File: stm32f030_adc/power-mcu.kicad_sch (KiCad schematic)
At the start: 24 parts, among them J4 Conn_01x05_Socket, U1 STM32F103C6Tx, U2 AMS1117-3.3, X1 USB_B_Micro, Y2 8 MHz

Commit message: [schematics] Impl |  Most of the work is done. Intermediate result
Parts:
- removed J4: Conn_01x05_Socket, Connector_PinHeader_2.00mm:PinHeader_1x05_P2.00mm_Vertical, symbol Connector:Conn_01x05_Socket
- added J1: Conn_01x03_Socket, Connector_PinHeader_1.00mm:PinHeader_1x03_P1.00mm_Vertical, symbol Connector:Conn_01x03_Socket
- added TP1, TP2: TestPoint, TestPoint:TestPoint_Pad_D2.0mm, symbol Connector:TestPoint
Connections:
- net GNDREF: now also J1.3 (Pin_3)
- net SWD_CLK: now also TP2.1
- net SWD_IO: now also TP1.1
- net USART_1_RX: now also J1.1 (Pin_1)
- net USART_1_TX: now also J1.2 (Pin_2)
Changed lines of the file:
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@@
 	(wire
 		(pts
+			(xy 219.71 120.65) (xy 229.87 120.65)
+		)
+		(stroke
+			(width 0)
+			(type default)
+		)
+	)
+	(wire
+		(pts
 			(xy 185.42 129.54) (xy 198.12 129.54)
 		)
@@
 	(wire
 		(pts
-			(xy 228.6 123.19) (xy 243.84 123.19)
+			(xy 229.87 123.19) (xy 222.25 123.19)
 		)
 		(stroke
@@
 	(wire
 		(pts
-			(xy 228.6 115.57) (xy 243.84 115.57)
-		)
-		(stroke
-			(width 0)
-			(type default)
-		)
-	)
-	(wire
-		(pts
 			(xy 193.04 82.55) (xy 207.01 82.55)
 		)
@@
 	(wire
 		(pts
-			(xy 228.6 118.11) (xy 243.84 118.11)
-		)
-		(stroke
-			(width 0)
-			(type default)
-		)
-	)
-	(wire
-		(pts
 			(xy 68.58 146.05) (xy 83.82 146.05)
 		)
@@
 	(wire
 		(pts
-			(xy 228.6 125.73) (xy 243.84 125.73)
-		)
-		(stroke
-			(width 0)
-			(type default)
-		)
-	)
-	(wire
-		(pts
 			(xy 44.45 59.69) (xy 44.45 60.96)
 		)
@@
 	(wire
 		(pts
-			(xy 228.6 120.65) (xy 243.84 120.65)
+			(xy 219.71 118.11) (xy 229.87 118.11)
 		)
 		(stroke
@@
 	(wire
 		(pts
+			(xy 222.25 123.19) (xy 222.25 124.46)
+		)
+		(stroke
+			(width 0)
+			(type default)
+		)
+	)
+	(wire
+		(pts
 			(xy 262.89 82.55) (xy 274.32 82.55)
 		)
@@
 		)
 	)
-	(label "USART_1_TX"
-		(at 240.03 115.57 180)
-		(fields_autoplaced yes)
-		(effects
-			(font
-				(size 1.27 1.27)
-			)
-			(justify right bottom)
-		)
-	)
 	(label "USB_D-"
 		(at 77.47 50.8 0)
@@
 		)
 	)
-	(label "USART_1_RX"
-		(at 240.03 118.11 180)
-		(fields_autoplaced yes)
-		(effects
-			(font
-				(size 1.27 1.27)
-			)
-			(justify right bottom)
-		)
-	)
 	(label "SWD_IO"
 		(at 198.12 129.54 180)
@@
 		)
 	)
-	(label "SWD_IO"
-		(at 234.95 120.65 180)
+	(label "USB_D-"
+		(at 198.12 124.46 180)
 		(fields_autoplaced yes)
 		(effects
@@
 		)
 	)
-	(label "USB_D-"
-		(at 198.12 124.46 180)
+	(label "USART_1_TX"
+		(at 227.33 120.65 180)
 		(fields_autoplaced yes)
 		(effects
@@
 	)
 	(label "SWD_CLK"
-		(at 237.49 123.19 180)
+		(at 198.12 132.08 180)
 		(fields_autoplaced yes)
 		(effects
@@
 		)
 	)
-	(label "SWD_CLK"
-		(at 198.12 132.08 180)
+	(label "USB_D+"
+		(at 198.12 127 180)
 		(fields_autoplaced yes)
 		(effects
@@
 		)
 	)
-	(label "USB_D+"
-		(at 198.12 127 180)
+	(label "USART_1_RX"
+		(at 227.33 118.11 180)
 		(fields_autoplaced yes)
 		(effects
@@
 	(symbol
 		(lib_id "power:GNDREF")
+		(at 222.25 124.46 0)
+		(unit 1)
+		(exclude_from_sim no)
+		(in_bom yes)
+		(on_board yes)
+		(dnp no)
+		(fields_autoplaced yes)
+		(property "Reference" "#PWR03"
+			(at 222.25 130.81 0)
+			(effects
+				(font
+					(size 1.27 1.27)
+				)
+				(hide yes)
+			)
+		)
+		(property "Value" "GNDREF"
+			(at 222.25 129.54 0)
+			(effects
+				(font
+					(size 1.27 1.27)
+				)
+			)
+		)
+		(property "Footprint" ""
+			(at 222.25 124.46 0)
+			(effects
+				(font
+					(size 1.27 1.27)
+				)
+				(hide yes)
+			)
+		)
+		(property "Datasheet" ""
+			(at 222.25 124.46 0)
+			(effects
+				(font
+					(size 1.27 1.27)
+				)
+				(hide yes)
+			)
+		)
+		(property "Description" ""
+			(at 222.25 124.46 0)
+			(effects
+				(font
+					(size 1.27 1.27)
+				)
+				(hide yes)
+			)
+		)
+		(pin "1"
+		)
+		(instances
+			(project "stm32f030_adc"
+				(path "/85629656-c73b-4e1f-b8e8-4366f4b01266/961be52f-ca6e-47db-97af-a75ea0ab8933"
+					(reference "#PWR03")
+					(unit 1)
+				)
+			)
+		)
+	)
+	(symbol
+		(lib_id "power:GNDREF")
 		(at 274.32 82.55 0)
 		(unit 1)
@@
 	)
 	(symbol
-		(lib_id "power:GNDREF")
-		(at 228.6 125.73 270)
+		(lib_id "Connector:Conn_01x03_Socket")
+		(at 234.95 120.65 0)
 		(unit 1)
 		(exclude_from_sim no)
@@
 		(dnp no)
 		(fields_autoplaced yes)
-		(property "Reference" "#PWR030"
-			(at 222.25 125.73 0)
+		(property "Reference" "J1"
+			(at 236.22 119.3799 0)
 			(effects
 				(font
 					(size 1.27 1.27)
 				)
-				(hide yes)
+				(justify left)
 			)
 		)
-		(property "Value" "GNDREF"
-			(at 224.79 125.7299 90)
+		(property "Value" "Conn_01x03_Socket"
+			(at 236.22 121.9199 0)
 			(effects
 				(font
 					(size 1.27 1.27)
 				)
-				(justify right)
+				(justify left)
 			)
 		)
-		(property "Footprint" ""
-			(at 228.6 125.73 0)
+		(property "Footprint" "Connector_PinHeader_1.00mm:PinHeader_1x03_P1.00mm_Vertical"
+			(at 234.95 120.65 0)
 			(effects
 				(font
@@
 			)
 		)
-		(property "Datasheet" ""
-			(at 228.6 125.73 0)
+		(property "Datasheet" "~"
+			(at 234.95 120.65 0)
 			(effects
 				(font
@@
 			)
 		)
-		(property "Description" ""
-			(at 228.6 125.73 0)
+		(property "Description" "Generic connector, single row, 01x03, script generated"
+			(at 234.95 120.65 0)
 			(effects
 				(font
@@
 			)
 		)
+		(pin "2"
+		)
+		(pin "3"
+		)
 		(pin "1"
 		)
 		(instances
-			(project "stm32f030_adc"
+			(project ""
 				(path "/85629656-c73b-4e1f-b8e8-4366f4b01266/961be52f-ca6e-47db-97af-a75ea0ab8933"
-					(reference "#PWR030")
+					(reference "J1")
 					(unit 1)
 				)
@@
 	)
 	(symbol
+		(lib_id "Connector:TestPoint")
+		(at 198.12 129.54 270)
+		(unit 1)
+		(exclude_from_sim no)
+		(in_bom yes)
+		(on_board yes)
+		(dnp no)
+		(property "Reference" "TP1"
+			(at 203.454 129.54 90)
+			(effects
+				(font
+					(size 1.27 1.27)
+				)
+				(justify left)
+			)
+		)
+		(property "Value" "TestPoint"
+			(at 203.2 130.8099 90)
+			(effects
+				(font
+					(size 1.27 1.27)
+				)
+				(justify left)
+				(hide yes)
+			)
+		)
+		(property "Footprint" "TestPoint:TestPoint_Pad_D2.0mm"
+			(at 198.12 134.62 0)
+			(effects
+				(font
+					(size 1.27 1.27)
+				)
+				(hide yes)
+			)
+		)
+		(property "Datasheet" "~"
+			(at 198.12 134.62 0)
+			(effects
+				(font
+					(size 1.27 1.27)
+				)
+				(hide yes)
+			)
+		)
+		(property "Description" "test point"
+			(at 198.12 129.54 0)
+			(effects
+				(font
+					(size 1.27 1.27)
+				)
+				(hide yes)
+			)
+		)
+		(pin "1"
+		)
+		(instances
+			(project ""
+				(path "/85629656-c73b-4e1f-b8e8-4366f4b01266/961be52f-ca6e-47db-97af-a75ea0ab8933"
+					(reference "TP1")
+					(unit 1)
+				)
+			)
+		)
+	)
+	(symbol
 		(lib_id "pspice:R")
 		(at 71.12 40.64 180)
@@
 	)
 	(symbol
-		(lib_id "Connector:Conn_01x05_Socket")
-		(at 248.92 120.65 0)
+		(lib_id "Connector:TestPoint")
+		(at 198.12 132.08 270)
 		(unit 1)
 		(exclude_from_sim no)
@@
 		(on_board yes)
 		(dnp no)
-		(fields_autoplaced yes)
-		(property "Reference" "J4"
-			(at 250.19 119.3799 0)
+		(property "Reference" "TP2"
+			(at 203.2 132.08 90)
 			(effects
 				(font
@@
 			)
 		)
-		(property "Value" "Conn_01x05_Socket"
-			(at 250.19 121.9199 0)
+		(property "Value" "TestPoint"
+			(at 203.2 133.3499 90)
 			(effects
 				(font
@@
 				)
 				(justify left)
+				(hide yes)
 			)
 		)
-		(property "Footprint" "Connector_PinHeader_2.00mm:PinHeader_1x05_P2.00mm_Vertical"
-			(at 248.92 120.65 0)
+		(property "Footprint" "TestPoint:TestPoint_Pad_D2.0mm"
+			(at 198.12 137.16 0)
 			(effects
 				(font
@@
 		)
 		(property "Datasheet" "~"
-			(at 248.92 120.65 0)
+			(at 198.12 137.16 0)
 			(effects
 				(font
@@
 			)
 		)
-		(property "Description" "Generic connector, single row, 01x05, script generated"
-			(at 248.92 120.65 0)
+		(property "Description" "test point"
+			(at 198.12 132.08 0)
 			(effects
 				(font
@@
 			)
 		)
-		(pin "2"
-		)
-		(pin "5"
-		)
-		(pin "4"
-		)
-		(pin "3"
-		)
 		(pin "1"
 		)
 		(instances
-			(project ""
+			(project "stm32f030_adc"
 				(path "/85629656-c73b-4e1f-b8e8-4366f4b01266/961be52f-ca6e-47db-97af-a75ea0ab8933"
-					(reference "J4")
+					(reference "TP2")
 					(unit 1)
 				)

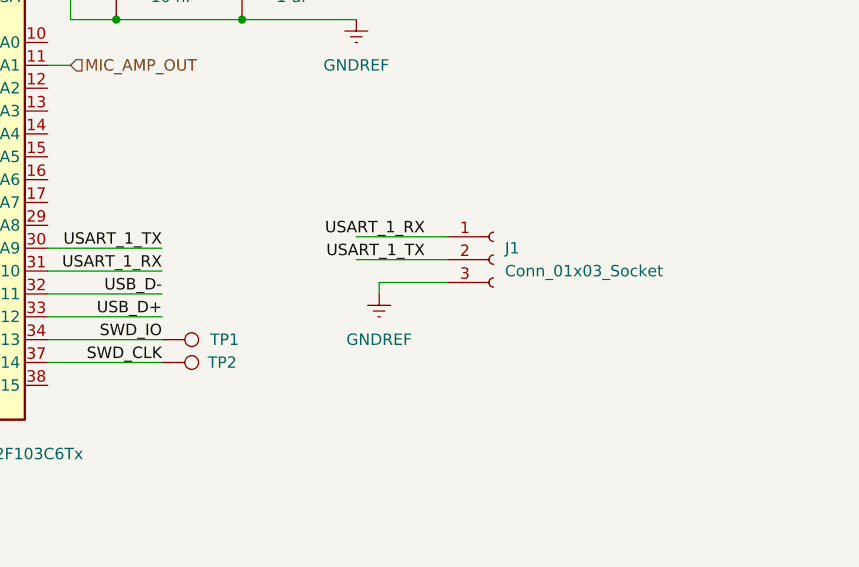
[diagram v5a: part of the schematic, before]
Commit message: Layout: 1-layer board, done, first approximation
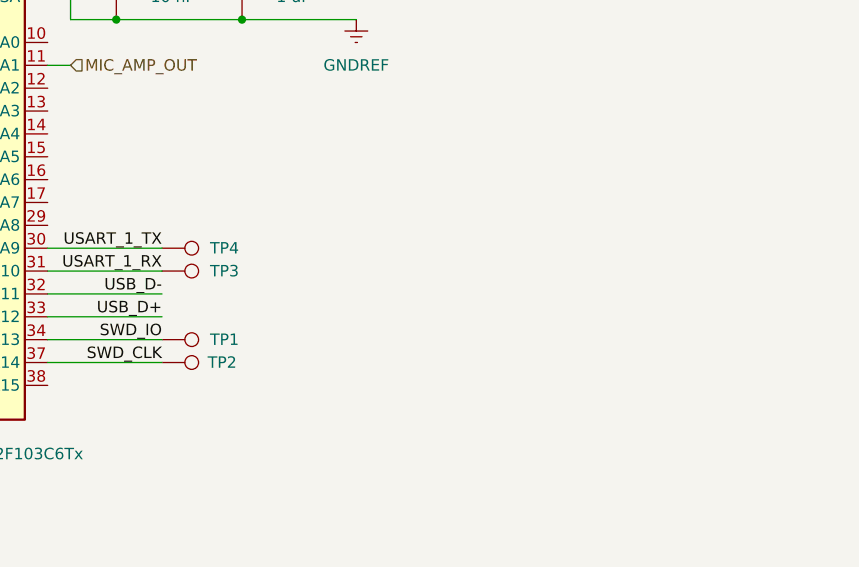
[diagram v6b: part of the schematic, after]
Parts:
- removed J1: Conn_01x03_Socket, Connector_PinHeader_1.00mm:PinHeader_1x03_P1.00mm_Vertical, symbol Connector:Conn_01x03_Socket
- added TP3, TP4: TestPoint, TestPoint:TestPoint_Pad_D2.0mm, symbol Connector:TestPoint
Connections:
- net USART_1_RX: now also TP3.1
- net USART_1_TX: now also TP4.1
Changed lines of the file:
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@@
-	(wire
-		(pts
-			(xy 219.71 120.65) (xy 229.87 120.65)
-		)
-		(stroke
-			(width 0)
-			(type default)
-		)
-	)
 	(wire
 		(pts
@@
 	(wire
 		(pts
-			(xy 229.87 123.19) (xy 222.25 123.19)
-		)
-		(stroke
-			(width 0)
-			(type default)
-		)
-	)
-	(wire
-		(pts
 			(xy 44.45 58.42) (xy 44.45 59.69)
 		)
@@
 	(wire
 		(pts
-			(xy 219.71 118.11) (xy 229.87 118.11)
-		)
-		(stroke
-			(width 0)
-			(type default)
-		)
-	)
-	(wire
-		(pts
 			(xy 55.88 43.18) (xy 52.07 43.18)
-		)
-		(stroke
-			(width 0)
-			(type default)
-		)
-	)
-	(wire
-		(pts
-			(xy 222.25 123.19) (xy 222.25 124.46)
 		)
 		(stroke
@@
 		)
 	)
-	(label "USART_1_TX"
-		(at 227.33 120.65 180)
+	(label "SWD_CLK"
+		(at 198.12 132.08 180)
 		(fields_autoplaced yes)
 		(effects
@@
 		)
 	)
-	(label "SWD_CLK"
-		(at 198.12 132.08 180)
-		(fields_autoplaced yes)
-		(effects
-			(font
-				(size 1.27 1.27)
-			)
-			(justify right bottom)
-		)
-	)
 	(label "USB_D+"
 		(at 198.12 127 180)
-		(fields_autoplaced yes)
-		(effects
-			(font
-				(size 1.27 1.27)
-			)
-			(justify right bottom)
-		)
-	)
-	(label "USART_1_RX"
-		(at 227.33 118.11 180)
 		(fields_autoplaced yes)
 		(effects
@@
 	(symbol
 		(lib_id "power:GNDREF")
-		(at 222.25 124.46 0)
-		(unit 1)
-		(exclude_from_sim no)
-		(in_bom yes)
-		(on_board yes)
-		(dnp no)
-		(fields_autoplaced yes)
-		(property "Reference" "#PWR03"
-			(at 222.25 130.81 0)
-			(effects
-				(font
-					(size 1.27 1.27)
-				)
-				(hide yes)
-			)
-		)
-		(property "Value" "GNDREF"
-			(at 222.25 129.54 0)
-			(effects
-				(font
-					(size 1.27 1.27)
-				)
-			)
-		)
-		(property "Footprint" ""
-			(at 222.25 124.46 0)
-			(effects
-				(font
-					(size 1.27 1.27)
-				)
-				(hide yes)
-			)
-		)
-		(property "Datasheet" ""
-			(at 222.25 124.46 0)
-			(effects
-				(font
-					(size 1.27 1.27)
-				)
-				(hide yes)
-			)
-		)
-		(property "Description" ""
-			(at 222.25 124.46 0)
-			(effects
-				(font
-					(size 1.27 1.27)
-				)
-				(hide yes)
-			)
-		)
-		(pin "1"
-		)
-		(instances
-			(project "stm32f030_adc"
-				(path "/85629656-c73b-4e1f-b8e8-4366f4b01266/961be52f-ca6e-47db-97af-a75ea0ab8933"
-					(reference "#PWR03")
-					(unit 1)
-				)
-			)
-		)
-	)
-	(symbol
-		(lib_id "power:GNDREF")
 		(at 274.32 82.55 0)
 		(unit 1)
@@
 	)
 	(symbol
-		(lib_id "Connector:Conn_01x03_Socket")
-		(at 234.95 120.65 0)
-		(unit 1)
-		(exclude_from_sim no)
-		(in_bom yes)
-		(on_board yes)
-		(dnp no)
-		(fields_autoplaced yes)
-		(property "Reference" "J1"
-			(at 236.22 119.3799 0)
-			(effects
-				(font
-					(size 1.27 1.27)
-				)
-				(justify left)
-			)
-		)
-		(property "Value" "Conn_01x03_Socket"
-			(at 236.22 121.9199 0)
-			(effects
-				(font
-					(size 1.27 1.27)
-				)
-				(justify left)
-			)
-		)
-		(property "Footprint" "Connector_PinHeader_1.00mm:PinHeader_1x03_P1.00mm_Vertical"
-			(at 234.95 120.65 0)
-			(effects
-				(font
-					(size 1.27 1.27)
-				)
-				(hide yes)
-			)
-		)
-		(property "Datasheet" "~"
-			(at 234.95 120.65 0)
-			(effects
-				(font
-					(size 1.27 1.27)
-				)
-				(hide yes)
-			)
-		)
-		(property "Description" "Generic connector, single row, 01x03, script generated"
-			(at 234.95 120.65 0)
-			(effects
-				(font
-					(size 1.27 1.27)
-				)
-				(hide yes)
-			)
-		)
-		(pin "2"
-		)
-		(pin "3"
-		)
-		(pin "1"
-		)
-		(instances
-			(project ""
-				(path "/85629656-c73b-4e1f-b8e8-4366f4b01266/961be52f-ca6e-47db-97af-a75ea0ab8933"
-					(reference "J1")
-					(unit 1)
-				)
-			)
-		)
-	)
-	(symbol
 		(lib_id "power:GNDREF")
 		(at 60.96 172.72 0)
@@
 	)
 	(symbol
+		(lib_id "Connector:TestPoint")
+		(at 198.12 119.38 270)
+		(unit 1)
+		(exclude_from_sim no)
+		(in_bom yes)
+		(on_board yes)
+		(dnp no)
+		(property "Reference" "TP4"
+			(at 203.454 119.38 90)
+			(effects
+				(font
+					(size 1.27 1.27)
+				)
+				(justify left)
+			)
+		)
+		(property "Value" "TestPoint"
+			(at 203.2 120.6499 90)
+			(effects
+				(font
+					(size 1.27 1.27)
+				)
+				(justify left)
+				(hide yes)
+			)
+		)
+		(property "Footprint" "TestPoint:TestPoint_Pad_D2.0mm"
+			(at 198.12 124.46 0)
+			(effects
+				(font
+					(size 1.27 1.27)
+				)
+				(hide yes)
+			)
+		)
+		(property "Datasheet" "~"
+			(at 198.12 124.46 0)
+			(effects
+				(font
+					(size 1.27 1.27)
+				)
+				(hide yes)
+			)
+		)
+		(property "Description" "test point"
+			(at 198.12 119.38 0)
+			(effects
+				(font
+					(size 1.27 1.27)
+				)
+				(hide yes)
+			)
+		)
+		(pin "1"
+		)
+		(instances
+			(project "stm32f030_adc"
+				(path "/85629656-c73b-4e1f-b8e8-4366f4b01266/961be52f-ca6e-47db-97af-a75ea0ab8933"
+					(reference "TP4")
+					(unit 1)
+				)
+			)
+		)
+	)
+	(symbol
 		(lib_id "Device:C")
 		(at 248.92 78.74 0)
@@
 					(unit 1)
 				)
+			)
+		)
+	)
+	(symbol
+		(lib_id "Connector:TestPoint")
+		(at 198.12 121.92 270)
+		(unit 1)
+		(exclude_from_sim no)
+		(in_bom yes)
+		(on_board yes)
+		(dnp no)
+		(property "Reference" "TP3"
+			(at 203.454 121.92 90)
+			(effects
+				(font
+					(size 1.27 1.27)
+				)
+				(justify left)
+			)
+		)
+		(property "Value" "TestPoint"
+			(at 203.2 123.1899 90)
+			(effects
+				(font
+					(size 1.27 1.27)
+				)
+				(justify left)
+				(hide yes)
+			)
+		)
+		(property "Footprint" "TestPoint:TestPoint_Pad_D2.0mm"
+			(at 198.12 127 0)
+			(effects
+				(font
+					(size 1.27 1.27)
+				)
+				(hide yes)
+			)
+		)
+		(property "Datasheet" "~"
+			(at 198.12 127 0)
+			(effects
+				(font
+					(size 1.27 1.27)
+				)
+				(hide yes)
+			)
+		)
+		(property "Description" "test point"
+			(at 198.12 121.92 0)
+			(effects
+				(font
+					(size 1.27 1.27)
+				)
+				(hide yes)
+			)
+		)
+		(pin "1"
+		)
+		(instances
+			(project "stm32f030_adc"
+				(path "/85629656-c73b-4e1f-b8e8-4366f4b01266/961be52f-ca6e-47db-97af-a75ea0ab8933"
+					(reference "TP3")
+					(unit 1)
+				)

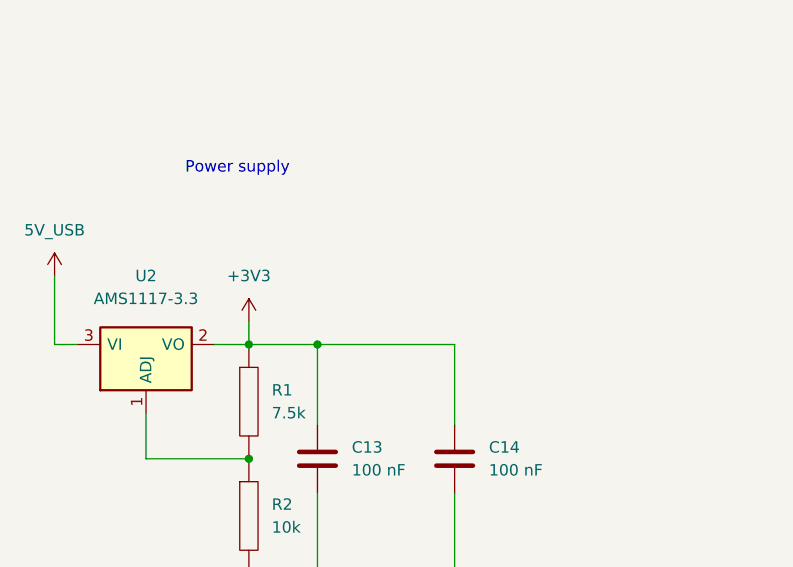
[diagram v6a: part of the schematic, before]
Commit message: Furhter fixes: added jumper for 3V3
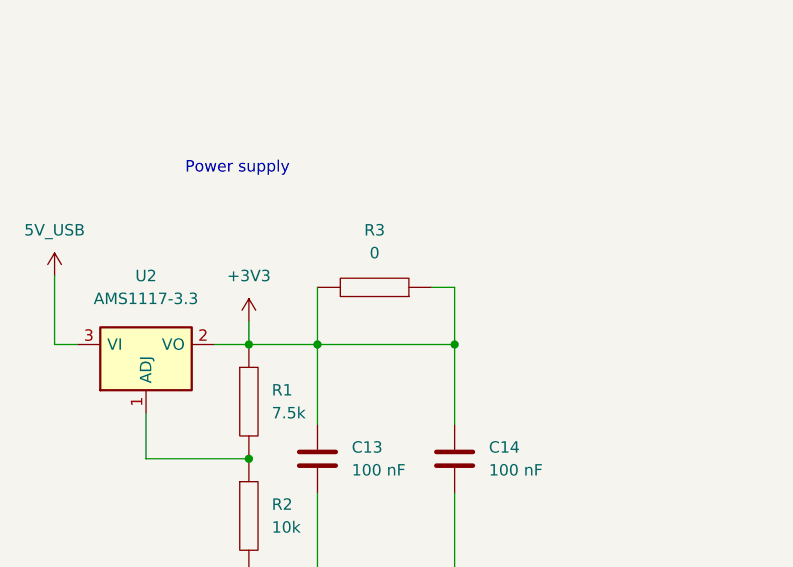
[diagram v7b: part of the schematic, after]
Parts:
- added R3: 0, Resistor_THT:R_Axial_DIN0207_L6.3mm_D2.5mm_P10.16mm_Horizontal, symbol pspice:R
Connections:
- net +3V3: now also R3.1, R3.2
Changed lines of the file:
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@@
 	)
 	(junction
+		(at 83.82 146.05)
+		(diameter 0)
+		(color 0 0 0 0)
+	)
+	(junction
 		(at 207.01 82.55)
 		(diameter 0)
@@
 	(wire
 		(pts
+			(xy 68.58 139.7) (xy 68.58 146.05)
+		)
+		(stroke
+			(width 0)
+			(type default)
+		)
+	)
+	(wire
+		(pts
 			(xy 121.92 59.69) (xy 128.27 59.69)
 		)
@@
 	(wire
 		(pts
+			(xy 83.82 146.05) (xy 83.82 154.94)
+		)
+		(stroke
+			(width 0)
+			(type default)
+		)
+	)
+	(wire
+		(pts
 			(xy 185.42 80.01) (xy 187.96 80.01)
 		)
@@
 	(wire
 		(pts
+			(xy 81.28 139.7) (xy 83.82 139.7)
+		)
+		(stroke
+			(width 0)
+			(type default)
+		)
+	)
+	(wire
+		(pts
 			(xy 187.96 88.9) (xy 187.96 86.36)
 		)
@@
 	(wire
 		(pts
-			(xy 83.82 146.05) (xy 83.82 154.94)
+			(xy 83.82 139.7) (xy 83.82 146.05)
 		)
 		(stroke
@@
 					(unit 1)
 				)
+			)
+		)
+	)
+	(symbol
+		(lib_id "pspice:R")
+		(at 74.93 139.7 270)
+		(mirror x)
+		(unit 1)
+		(exclude_from_sim no)
+		(in_bom yes)
+		(on_board yes)
+		(dnp no)
+		(property "Reference" "R3"
+			(at 74.93 133.35 90)
+			(effects
+				(font
+					(size 1.27 1.27)
+				)
+			)
+		)
+		(property "Value" "0"
+			(at 74.93 135.89 90)
+			(effects
+				(font
+					(size 1.27 1.27)
+				)
+			)
+		)
+		(property "Footprint" "Resistor_THT:R_Axial_DIN0207_L6.3mm_D2.5mm_P10.16mm_Horizontal"
+			(at 74.93 139.7 0)
+			(effects
+				(font
+					(size 1.27 1.27)
+				)
+				(hide yes)
+			)
+		)
+		(property "Datasheet" "~"
+			(at 74.93 139.7 0)
+			(effects
+				(font
+					(size 1.27 1.27)
+				)
+				(hide yes)
+			)
+		)
+		(property "Description" ""
+			(at 74.93 139.7 0)
+			(effects
+				(font
+					(size 1.27 1.27)
+				)
+				(hide yes)
+			)
+		)
+		(pin "1"
+		)
+		(pin "2"
+		)
+		(instances
+			(project "stm32f030_adc"
+				(path "/85629656-c73b-4e1f-b8e8-4366f4b01266/961be52f-ca6e-47db-97af-a75ea0ab8933"
+					(reference "R3")
+					(unit 1)
+				)
